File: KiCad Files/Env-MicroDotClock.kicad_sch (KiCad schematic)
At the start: 40 parts, among them IC1 IS31FL3730-QFLS2-TR, IC2 IS31FL3730-QFLS2-TR, IC3 IS31FL3730-QFLS2-TR, IC4 IS31FL3730-QFLS2-TR, M1 Dip-14 Socket, M2 Dip-14 Socket, M3 Dip-14 Socket, M4 Dip-14 Socket, M5 Dip-14 Socket, M6 Dip-14 Socket, M7 Dip-14 Socket, M8 Dip-14 Socket, Q1 2SC1815, SW1 SKRK, SW2 SKRK, SW3 SKRK, SW4 SKRK, SW5 DIP SPST W5.08mm_P1.27mm, U1 Raspberry Pi Pico, U3 DS3231M

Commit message: Fixed pullups, they ran to 5V instead of 3.3V meaning they would fry the MCU pins eventually
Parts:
- R1, R2: value 0805 2.2K -> 0805 10K
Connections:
- net +5V: no longer R1.1, R2.1
- net +3V3: now reaches U1.36 (3V3)
- net +3V3: now also R1.1, R2.1
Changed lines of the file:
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@@
-    )
-  )
-  (symbol (lib_id "power:+5V") (at 101.6 151.13 0) (unit 1)
-    (in_bom yes) (on_board yes) (dnp no) (fields_autoplaced)
-    (property "Reference" "#PWR039" (at 101.6 154.94 0)
-      (effects (font (size 1.27 1.27)) hide)
-    )
-    (property "Value" "+5V" (at 101.6 147.955 0)
-      (effects (font (size 1.27 1.27)))
-    )
-    (property "Footprint" "" (at 101.6 151.13 0)
-      (effects (font (size 1.27 1.27)) hide)
-    )
-    (property "Datasheet" "" (at 101.6 151.13 0)
-      (effects (font (size 1.27 1.27)) hide)
-    )
-    (pin "1")
-    (instances
-      (project "Env-MicroDotClock"
-        (path "/3dbeb8d8-208e-4f6d-8d30-b14372f68a4f"
-          (reference "#PWR039") (unit 1)
-        )
-      )
     )
   )
@@
       (effects (font (size 1.27 1.27)) (justify left))
     )
-    (property "Value" "0805 2.2K" (at 104.14 156.21 0)
+    (property "Value" "0805 10K" (at 104.14 156.21 0)
       (effects (font (size 1.27 1.27)) (justify left))
     )
@@
       (effects (font (size 1.27 1.27)) (justify left))
     )
-    (property "Value" "0805 2.2K" (at 101.6 157.48 0)
+    (property "Value" "0805 10K" (at 101.6 157.48 0)
       (effects (font (size 1.27 1.27)) (justify left))
     )
@@
     )
   )
+  (symbol (lib_id "power:+3V3") (at 101.6 151.13 0) (unit 1)
+    (in_bom yes) (on_board yes) (dnp no) (fields_autoplaced)
+    (property "Reference" "#PWR044" (at 101.6 154.94 0)
+      (effects (font (size 1.27 1.27)) hide)
+    )
+    (property "Value" "+3V3" (at 101.6 146.685 0)
+      (effects (font (size 1.27 1.27)))
+    )
+    (property "Footprint" "" (at 101.6 151.13 0)
+      (effects (font (size 1.27 1.27)) hide)
+    )
+    (property "Datasheet" "" (at 101.6 151.13 0)
+      (effects (font (size 1.27 1.27)) hide)
+    )
+    (pin "1")
+    (instances
+      (project "Env-MicroDotClock"
+        (path "/3dbeb8d8-208e-4f6d-8d30-b14372f68a4f"
+          (reference "#PWR044") (unit 1)
+        )
+      )
+    )
+  )
   (symbol (lib_id "power:GND") (at 194.945 149.86 0) (mirror y) (unit 1)
     (in_bom yes) (on_board yes) (dnp no) (fields_autoplaced)
@@
         )
       )
+    )
+  )
+  (symbol (lib_id "power:+3V3") (at 32.385 150.495 0) (unit 1)
+    (in_bom yes) (on_board yes) (dnp no) (fields_autoplaced)
+    (property "Reference" "#PWR039" (at 32.385 154.305 0)
+      (effects (font (size 1.27 1.27)) hide)
+    )
+    (property "Value" "+3V3" (at 32.385 146.05 0)
+      (effects (font (size 1.27 1.27)))
+    )
+    (property "Footprint" "" (at 32.385 150.495 0)
+      (effects (font (size 1.27 1.27)) hide)
+    )
+    (property "Datasheet" "" (at 32.385 150.495 0)
+      (effects (font (size 1.27 1.27)) hide)
+    )
+    (pin "1")
+    (instances
+      (project "Env-MicroDotClock"
+        (path "/3dbeb8d8-208e-4f6d-8d30-b14372f68a4f"
+          (reference "#PWR039") (unit 1)
+        )
+      )

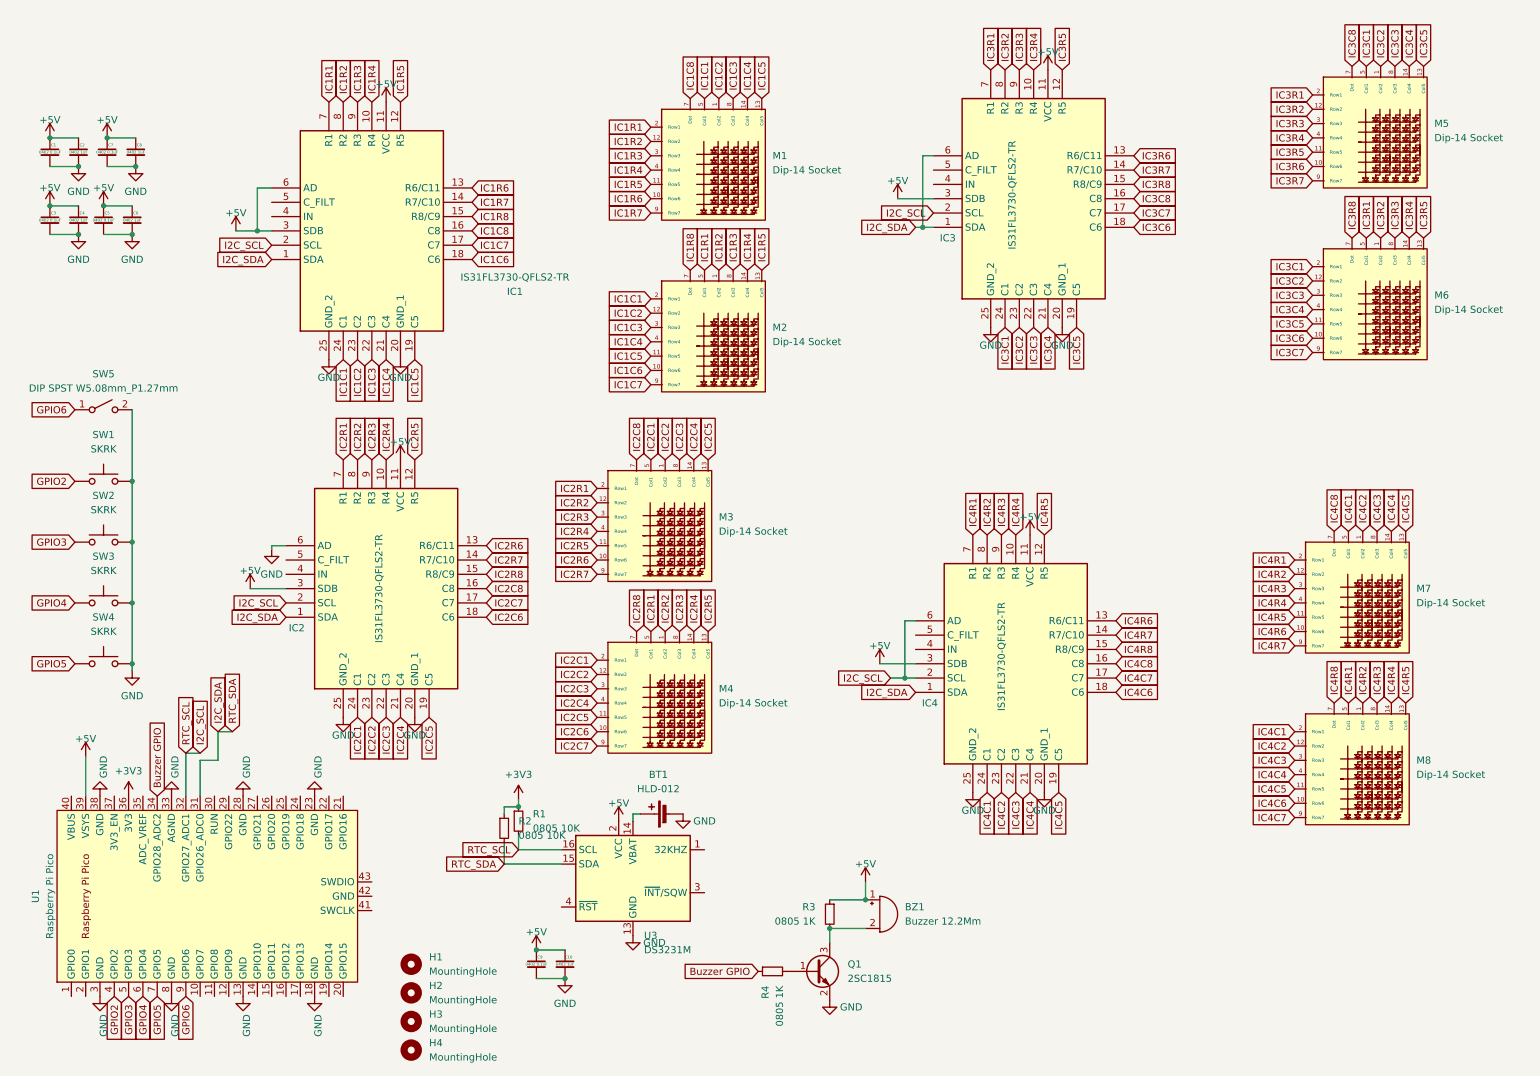
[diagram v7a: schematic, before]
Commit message: swapped 5V for 3V3 as per information on the datasheet
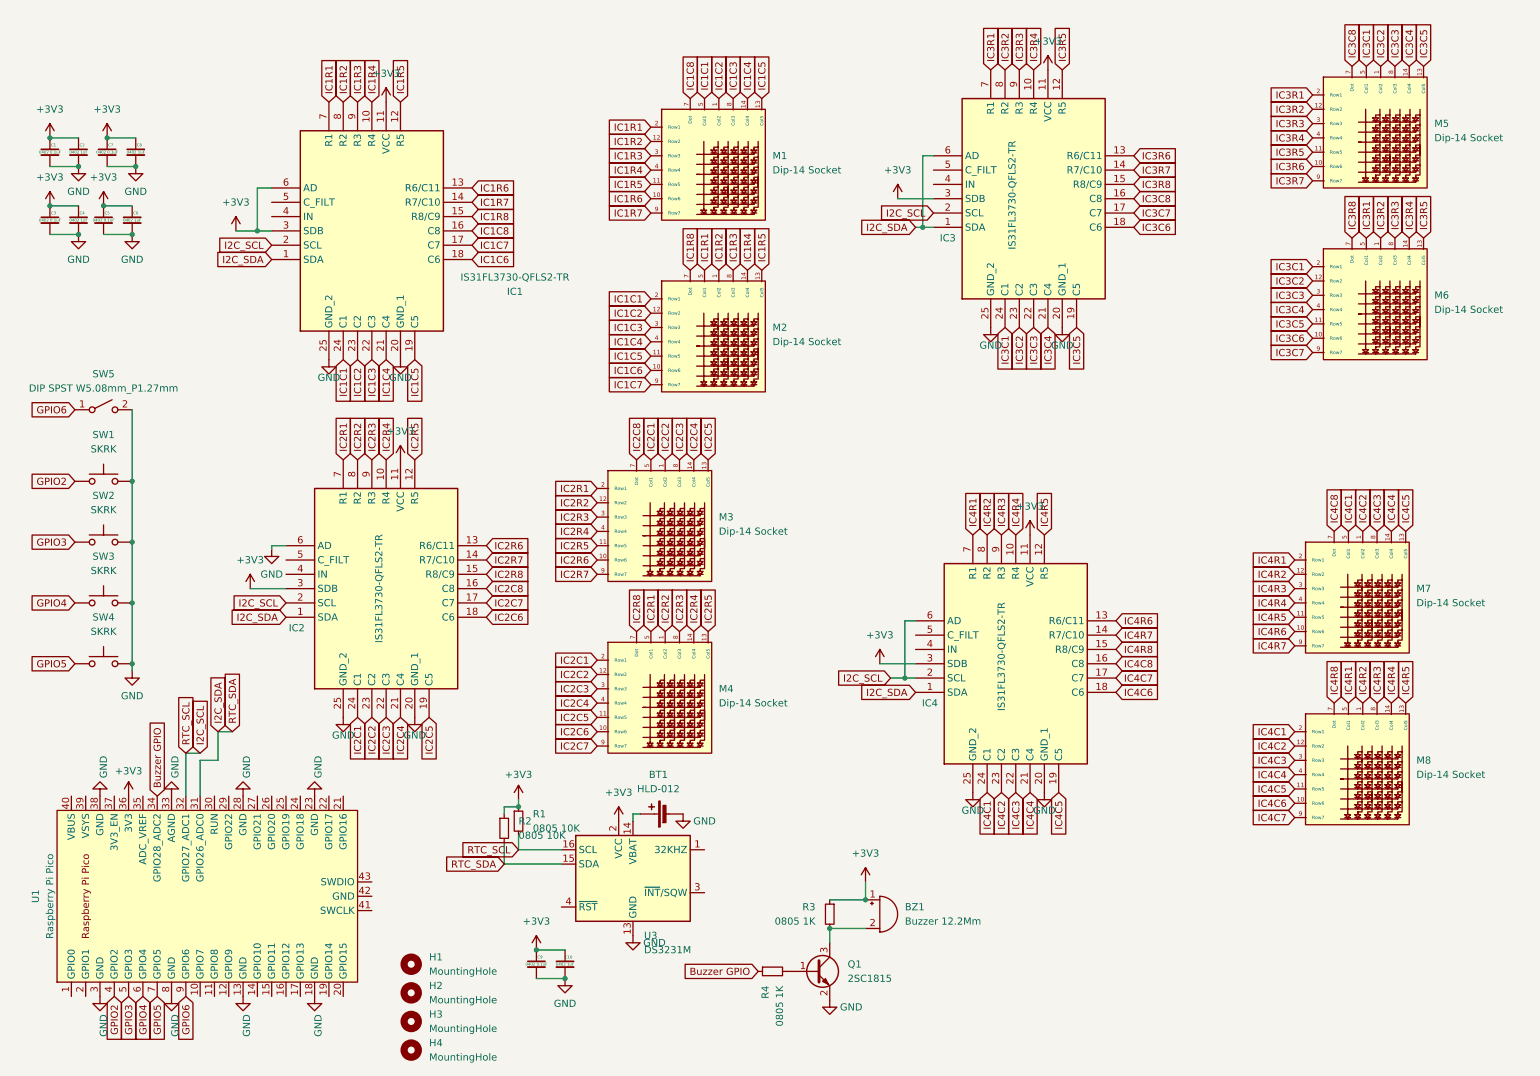
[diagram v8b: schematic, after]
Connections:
- net +3V3: now also BZ1.1 (-), C1.1, C10.1, C2.1, C3.1, C4.1, C5.1, C6.1, C7.1, C8.1, C9.1, IC1.11 (VCC), IC1.3 (SDB), IC1.6 (AD), IC2.11 (VCC), IC2.3 (SDB), IC3.11 (VCC), IC3.3 (SDB), IC4.11 (VCC), IC4.3 (SDB), R3.1, U3.2 (VCC)
- removed net +5V: BZ1.1 (-), C1.1, C10.1, C2.1, C3.1, C4.1, C5.1, C6.1, C7.1, C8.1, C9.1, IC1.11 (VCC), IC1.3 (SDB), IC1.6 (AD), IC2.11 (VCC), IC2.3 (SDB), IC3.11 (VCC), IC3.3 (SDB), IC4.11 (VCC), IC4.3 (SDB), R3.1, U1.39 (VSYS), U3.2 (VCC)
